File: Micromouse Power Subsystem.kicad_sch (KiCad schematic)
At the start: 9 parts, among them IC1 CH224K, J1 TYPEC-304-ACP16, J2 Conn_02x16_Odd_Even, U1 INA219AIDCNR

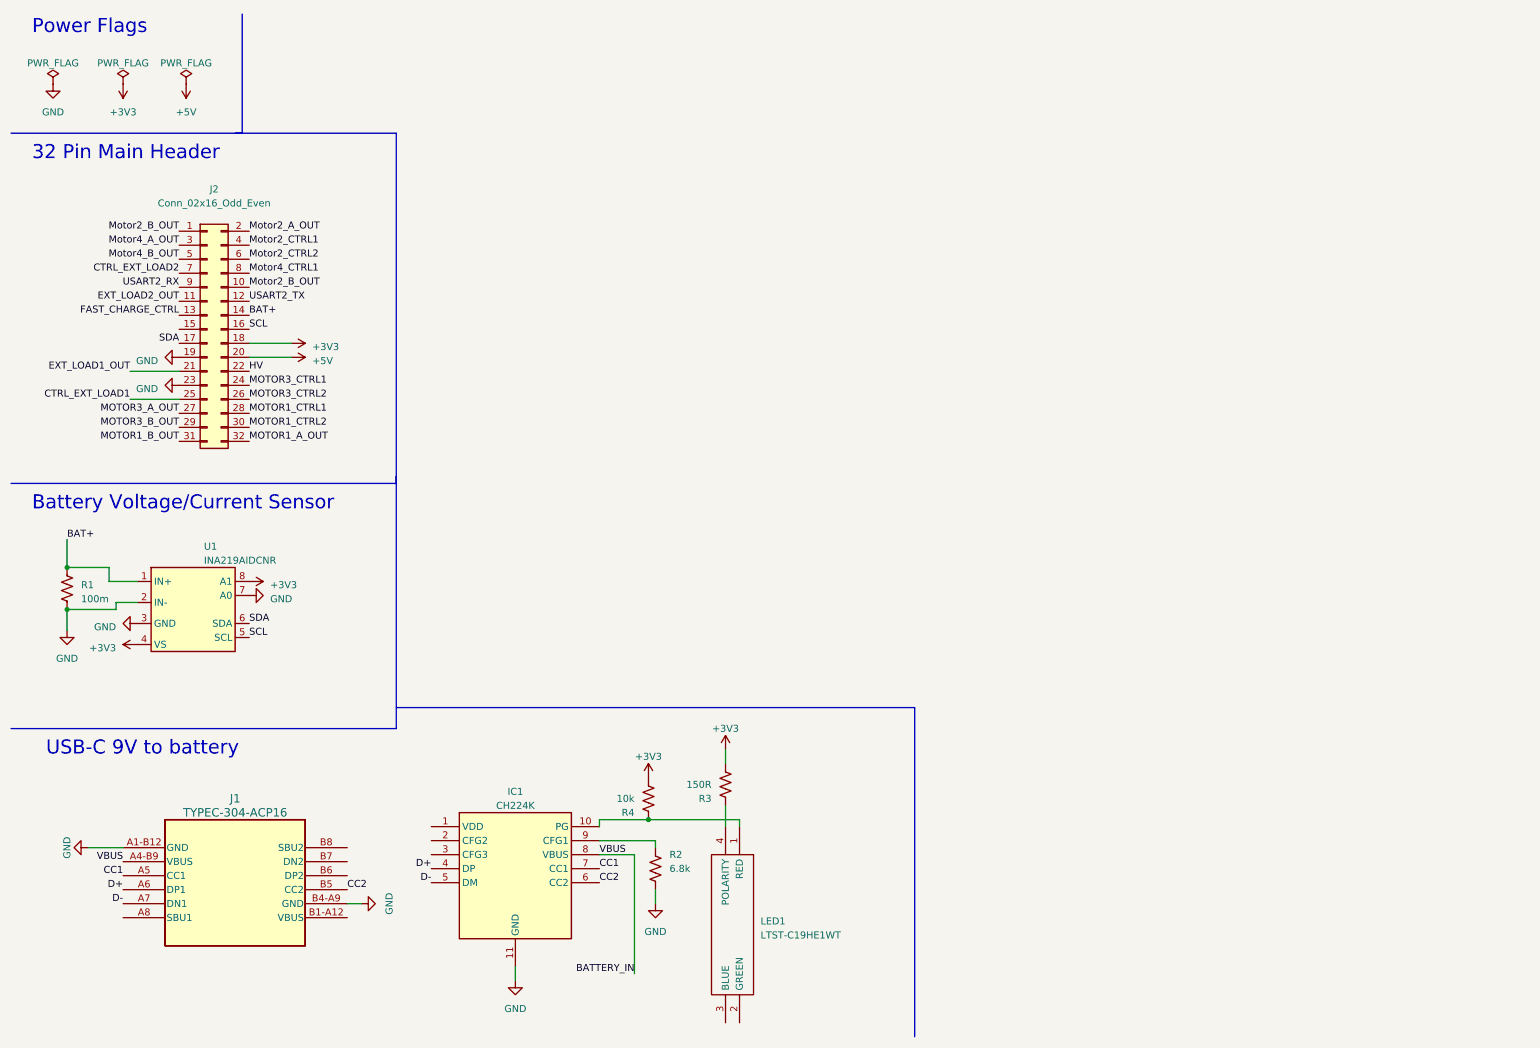
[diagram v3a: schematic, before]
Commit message: Added the charging modes as well as the charger powering the circuit when plugged in.
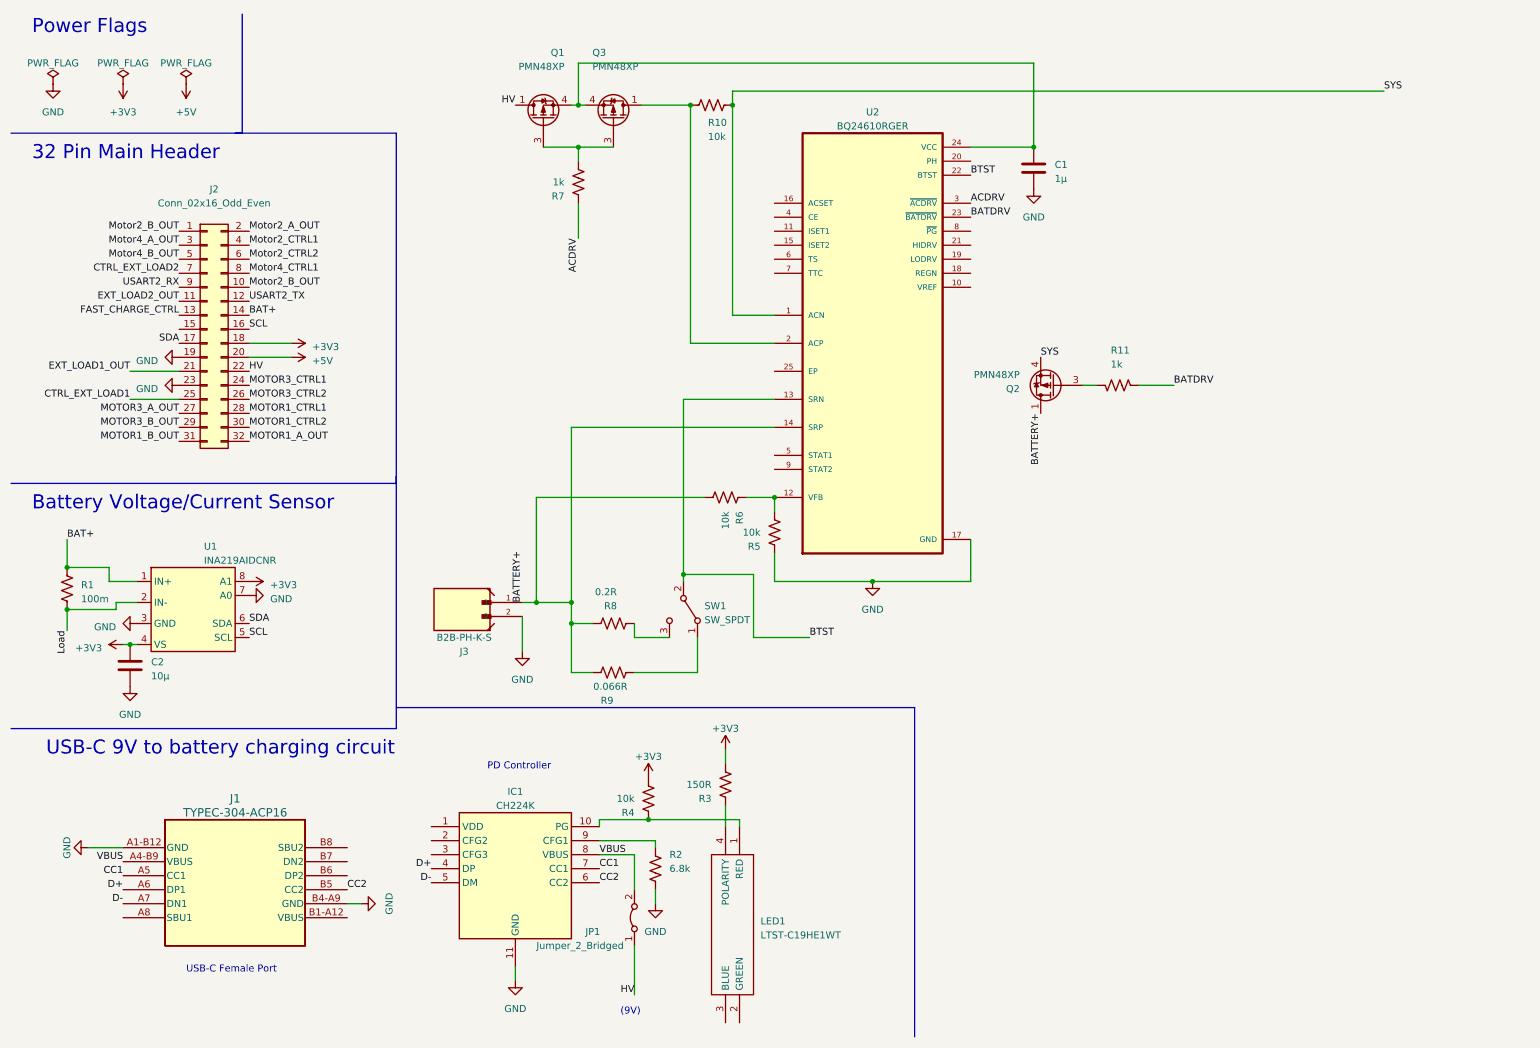
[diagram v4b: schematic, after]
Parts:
- added C1: 1µ, symbol Device:C
- added C2: 10µ, symbol Device:C
- added J3: B2B-PH-K-S, Battery JST Connector:JST_B2B-PH-K-S, symbol B2B-PH-K-S:B2B-PH-K-S
- added JP1: Jumper_2_Bridged, Jumper:SolderJumper-2_P1.3mm_Bridged2Bar_Pad1.0x1.5mm, symbol Jumper:Jumper_2_Bridged
- added Q1, Q2, Q3: PMN48XP, Package_SO:TSOP-6_1.65x3.05mm_P0.95mm, symbol Transistor_FET:PMN48XP
- added R10, R5, R6: 10k, Resistor_THT:R_Axial_DIN0204_L3.6mm_D1.6mm_P1.90mm_Vertical, symbol Device:R_US
- added R11, R7: 1k, Resistor_THT:R_Axial_DIN0204_L3.6mm_D1.6mm_P1.90mm_Vertical, symbol Device:R_US
- added R8: 0.2R, Resistor_THT:R_Axial_DIN0204_L3.6mm_D1.6mm_P1.90mm_Vertical, symbol Device:R_US
- added R9: 0.066R, Resistor_THT:R_Axial_DIN0204_L3.6mm_D1.6mm_P1.90mm_Vertical, symbol Device:R_US
- added SW1: SW_SPDT, symbol Switch:SW_SPDT
- added U2: BQ24610RGER, Battery Charger:QFN50P400X400X100-25N, symbol BQ24610RGER:BQ24610RGER
- U1: footprint Package_SO:SOIC-8_3.9x4.9mm_P1.27mm -> INA219:SOT65P280X145-8N
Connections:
- net +3V3: now also C2.1
- net GND: now also C1.2, C2.2, J3.2, R5.2, U2.17 (GND); no longer R1.1, U1.2 (IN-)
- net HV: now also JP1.1 (A), Q1.1 (D), Q1.2 (D), Q1.5 (D), Q1.6 (D)
- net BATTERY_IN renamed VBUS
- net VBUS: now also JP1.2 (B)
- new net: Q1.3 (G), Q3.3 (G), R7.1
- new net: R5.1, R6.2, U2.12 (VFB)
- new net: C1.1, Q1.4 (S), Q3.4 (S), U2.24 (VCC)
- new net: Q2.3 (G), R11.1
- new net: R9.1, SW1.1 (A)
- new net: R8.1, SW1.3 (C)
- new net: Q3.1 (D), Q3.2 (D), Q3.5 (D), Q3.6 (D), R10.1, U2.2 (ACP)
- new net ACDRV: R7.2, U2.3 (~{ACDRV})
- new net BATDRV: R11.2, U2.23 (~{BATDRV})
- new net BATTERY+: J3.1, Q2.1 (D), Q2.2 (D), Q2.5 (D), Q2.6 (D), R6.1, R8.2, R9.2, U2.14 (SRP)
- new net BTST: SW1.2 (B), U2.13 (SRN), U2.22 (BTST)
- new net Load: R1.1, U1.2 (IN-)
- new net SYS: Q2.4 (S), R10.2, U2.1 (ACN)
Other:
- note added: "(9V)"
- note added: "PD Controller"
- note added: "USB-C 9V to battery charging circuit"
- note added: "USB-C Female Port"
- note removed: "USB-C 9V to battery"

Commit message: Added the remaining connections to ground that were not in use for the battery charger
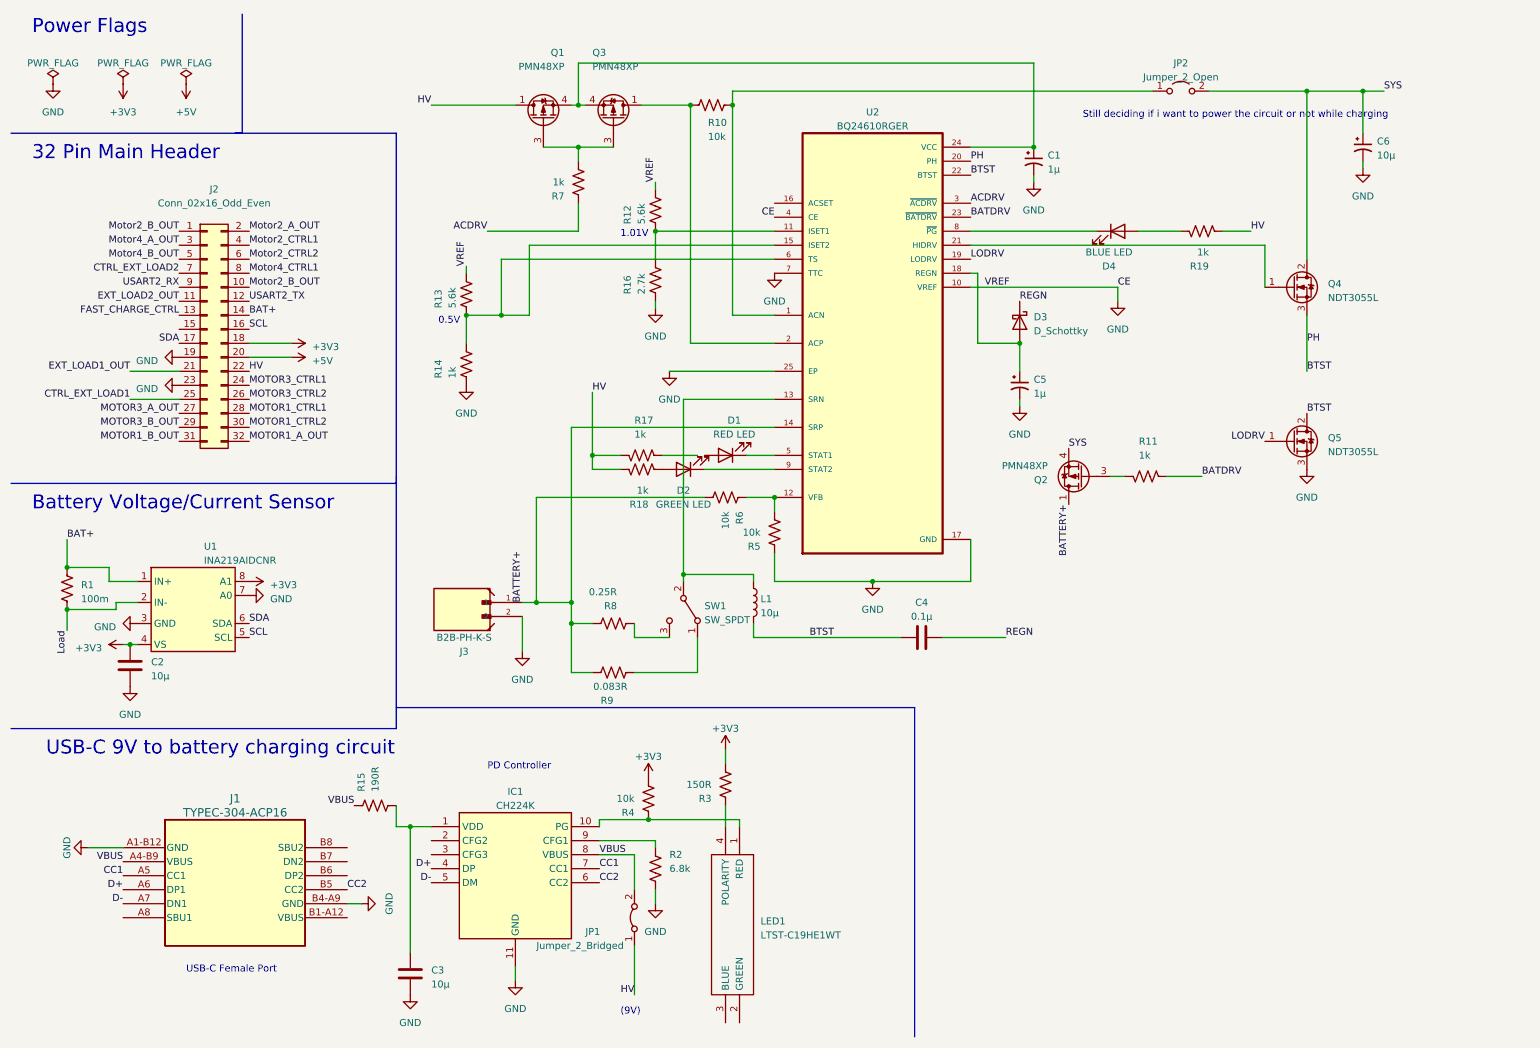
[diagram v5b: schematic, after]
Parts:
- removed C1: 1µ, symbol Device:C
- added C1, C5: 1µ, symbol Device:C_Polarized_Small_US
- added C3: 10µ, symbol Device:C
- added C4: 0.1µ, symbol Device:C
- added C6: 10µ, symbol Device:C_Polarized_Small_US
- added D1: RED LED, symbol Device:LED
- added D2: GREEN LED, symbol Device:LED
- added D3: D_Schottky, symbol Device:D_Schottky
- added D4: BLUE LED, symbol Device:LED
- added JP2: Jumper_2_Open, symbol Jumper:Jumper_2_Open
- added L1: 10µ, symbol Device:L
- added Q4, Q5: NDT3055L, Package_TO_SOT_SMD:SOT-223-3_TabPin2, symbol Transistor_FET:NDT3055L
- added R12, R13: 5.6k, Resistor_THT:R_Axial_DIN0204_L3.6mm_D1.6mm_P1.90mm_Vertical, symbol Device:R_US
- added R14, R17, R18, R19: 1k, Resistor_THT:R_Axial_DIN0204_L3.6mm_D1.6mm_P1.90mm_Vertical, symbol Device:R_US
- added R15: 190R, Resistor_THT:R_Axial_DIN0204_L3.6mm_D1.6mm_P1.90mm_Vertical, symbol Device:R_US
- added R16: 2.7k, Resistor_THT:R_Axial_DIN0204_L3.6mm_D1.6mm_P1.90mm_Vertical, symbol Device:R_US
- R8: value 0.2R -> 0.25R
- R9: value 0.066R -> 0.083R
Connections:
- net BTST: now also U2.20 (PH), C4.1, L1.2, Q4.3 (S), Q5.2 (D); no longer SW1.2 (B), U2.13 (SRN)
- net GND: now also U2.10 (VREF), U2.25 (EP), U2.4 (CE), U2.7 (TTC), C1.2, C3.2, C5.2, C6.2, Q5.3 (S), R12.2, R13.2, R14.1, R16.1
- net HV: now also R17.1, R18.2, R19.1
- net SYS: now also C6.1, JP2.2 (B), Q4.2 (D); no longer R10.2, U2.1 (ACN)
- net VBUS: now also R15.2
- net at Q1.4 (S), Q3.4 (S), U2.24 (VCC): now also C1.1
- net at U2.11 (ISET1): now also R12.1, R16.2
- net at U2.15 (ISET2): now also U2.6 (TS), R13.1, R14.2
- net at U2.18 (REGN): now also C5.1, D3.2 (A)
- net LODRV: now reaches U2.19 (LODRV)
- net LODRV: now also Q5.1 (G)
- net at U2.21 (HIDRV): now also Q4.1 (G)
- net at U2.5 (STAT1): now also D1.1 (K)
- net at U2.8 (~{PG}): now also D4.1 (K)
- net at U2.9 (STAT2): now also D2.1 (K)
- net at IC1.1 (VDD): now also C3.1, R15.1
- new net: D2.2 (A), R18.1
- new net: JP2.1 (A), R10.2, U2.1 (ACN)
- new net: L1.1, SW1.2 (B), U2.13 (SRN)
- new net: D4.2 (A), R19.2
- new net REGN: C4.2, D3.1 (K)
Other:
- note added: "0.5V"
- note added: "1.01V"
- note added: "Still deciding if i want to power the circuit or not while charging"
- moved on the sheet: Q2, R11

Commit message: Added charging circuit with new IC (BQ24074RGTR)
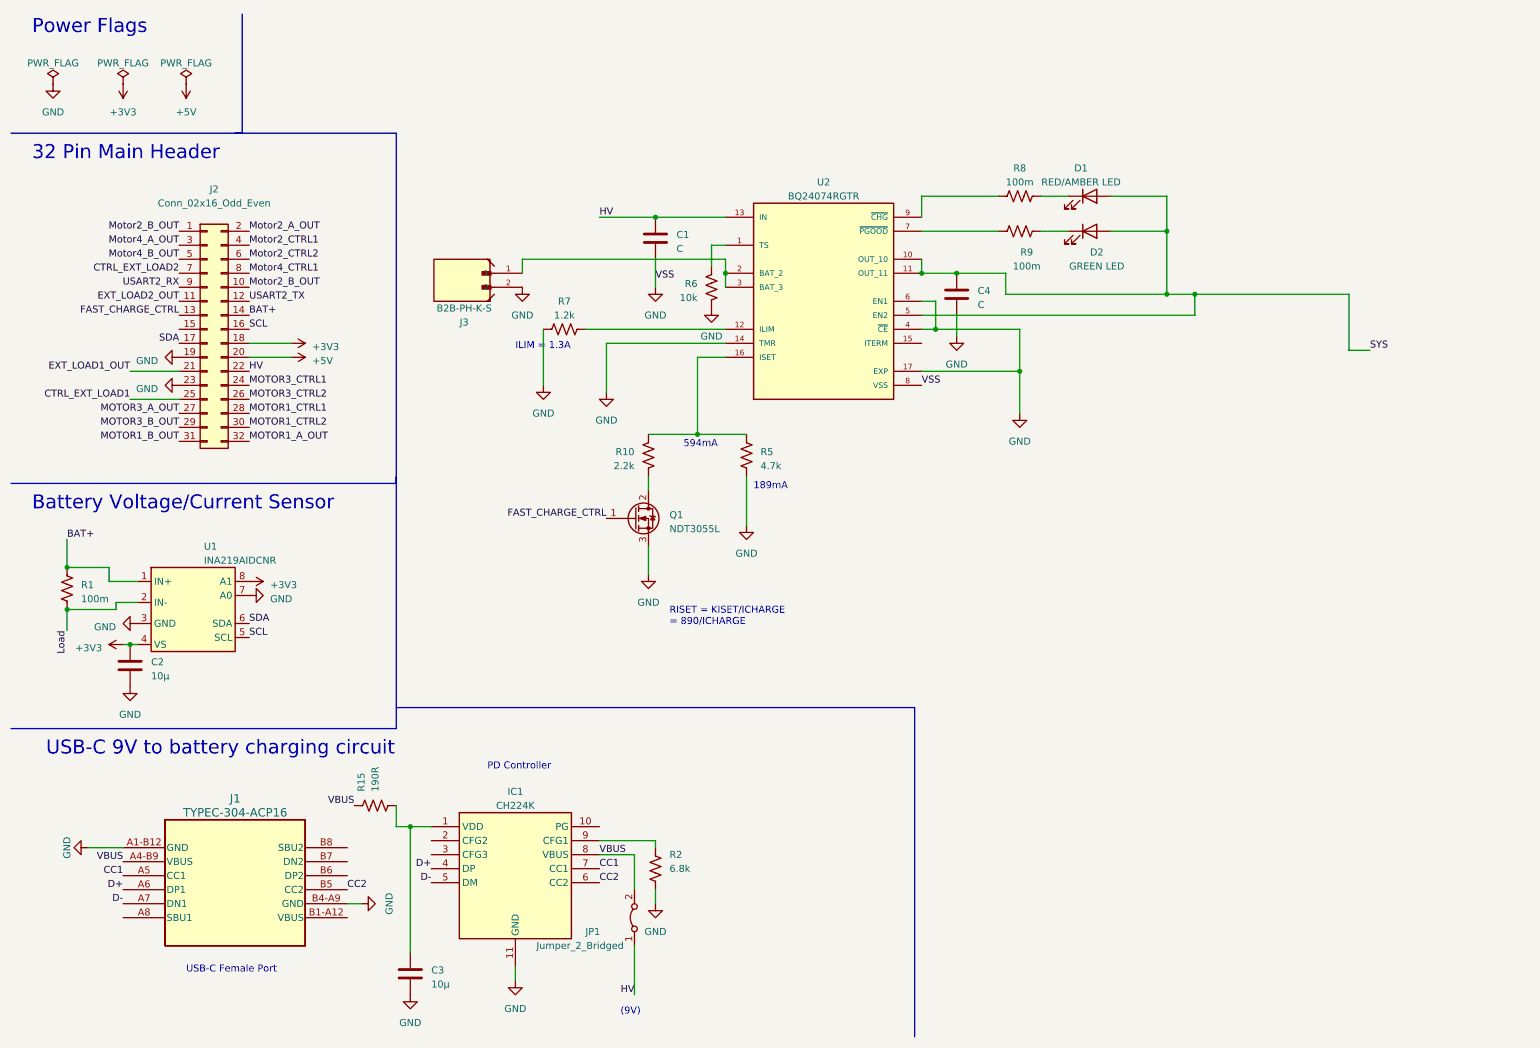
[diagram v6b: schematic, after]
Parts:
- removed C1, C5: 1µ, symbol Device:C_Polarized_Small_US
- removed C6: 10µ, symbol Device:C_Polarized_Small_US
- removed D3: D_Schottky, symbol Device:D_Schottky
- removed D4: BLUE LED, symbol Device:LED
- removed JP2: Jumper_2_Open, symbol Jumper:Jumper_2_Open
- removed L1: 10µ, symbol Device:L
- removed LED1: LTST-C19HE1WT, RGB LED:LTST-C19HE1WT, symbol LTST-C19HE1WT:LTST-C19HE1WT
- removed Q1, Q2, Q3: PMN48XP, Package_SO:TSOP-6_1.65x3.05mm_P0.95mm, symbol Transistor_FET:PMN48XP
- removed Q4, Q5: NDT3055L, Package_TO_SOT_SMD:SOT-223-3_TabPin2, symbol Transistor_FET:NDT3055L
- removed R11, R14, R17, R18, R19: 1k, Resistor_THT:R_Axial_DIN0204_L3.6mm_D1.6mm_P1.90mm_Vertical, symbol Device:R_US
- removed R12, R13: 5.6k, Resistor_THT:R_Axial_DIN0204_L3.6mm_D1.6mm_P1.90mm_Vertical, symbol Device:R_US
- removed R16: 2.7k, Resistor_THT:R_Axial_DIN0204_L3.6mm_D1.6mm_P1.90mm_Vertical, symbol Device:R_US
- removed R3: 150R, Resistor_THT:R_Axial_DIN0204_L3.6mm_D1.6mm_P1.90mm_Vertical, symbol Device:R_US
- removed R4: 10k, Resistor_THT:R_Axial_DIN0204_L3.6mm_D1.6mm_P1.90mm_Vertical, symbol Device:R_US
- removed SW1: SW_SPDT, symbol Switch:SW_SPDT
- removed U2: BQ24610RGER, Battery Charger:QFN50P400X400X100-25N, symbol BQ24610RGER:BQ24610RGER
- added C1: C, symbol Device:C
- added Q1: NDT3055L, Package_TO_SOT_SMD:SOT-223-3_TabPin2, symbol Transistor_FET:NDT3055L
- added U2: BQ24074RGTR, BQ24074RGTR:QFN50P300X300X100-17N, symbol BQ24074RGTR:BQ24074RGTR
- C4: value 0.1µ -> C
- D1: value RED LED -> RED/AMBER LED
- J3: footprint Battery JST Connector:JST_B2B-PH-K-S -> B2B-PH-K-S:JST_B2B-PH-K-S
- R10: value 10k -> 2.2k; footprint Resistor_THT:R_Axial_DIN0204_L3.6mm_D1.6mm_P1.90mm_Vertical -> Resistor_SMD:R_Shunt_Ohmite_LVK12
- R5: value 10k -> 4.7k; footprint Resistor_THT:R_Axial_DIN0204_L3.6mm_D1.6mm_P1.90mm_Vertical -> Resistor_SMD:R_Shunt_Ohmite_LVK12
- R6: footprint Resistor_THT:R_Axial_DIN0204_L3.6mm_D1.6mm_P1.90mm_Vertical -> Resistor_SMD:R_Shunt_Ohmite_LVK12
- R7: value 1k -> 1.2k; footprint Resistor_THT:R_Axial_DIN0204_L3.6mm_D1.6mm_P1.90mm_Vertical -> Resistor_SMD:R_Shunt_Ohmite_LVK12
- R8: value 0.25R -> 100m; footprint Resistor_THT:R_Axial_DIN0204_L3.6mm_D1.6mm_P1.90mm_Vertical -> Resistor_SMD:R_Shunt_Ohmite_LVK12
- R9: value 0.083R -> 100m; footprint Resistor_THT:R_Axial_DIN0204_L3.6mm_D1.6mm_P1.90mm_Vertical -> Resistor_SMD:R_Shunt_Ohmite_LVK12
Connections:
- net BTST is gone; now on net SYS: C4.1
- net REGN is gone; now on net GND: C4.2
- net FAST_CHARGE_CTRL: now also Q1.1 (G)
- net GND: now also R5.1, R6.1, R7.1, C1.2, Q1.3 (S), U2.14 (TMR), U2.17 (EXP), U2.4 (~{CE}), U2.6 (EN1), U2.8 (VSS); no longer R5.2
- net HV: now also C1.1, U2.13 (IN)
- net SYS: now also D1.2 (A), D2.2 (A), U2.10 (OUT_10), U2.11 (OUT_11), U2.5 (EN2)
- net at D2.1 (K): now also R9.2
- net at R6.2: now also U2.1 (TS); no longer R5.1
- net at R10.2: now also R5.2, U2.16 (ISET)
- net at R9.1: now also U2.7 (~{PGOOD})
- net at R8.1: now also D1.1 (K)
- net at R10.1: now also Q1.2 (D)
- net ACDRV: no longer names the net of R7.2
- net ACDRV: now also U2.12 (ILIM)
- removed net BATTERY+: J3.1, R6.1, R8.2, R9.2
- new net: J3.1, U2.2 (BAT_2), U2.3 (BAT_3)
- new net: R8.2, U2.9 (~{CHG})
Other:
- note added: "189mA"
- note added: "594mA"
- note added: "ILIM = 1.3A"
- note added: "RISET = KISET/ICHARGE = 890/ICHARGE"
- note removed: "0.5V"
- note removed: "1.01V"
- note removed: "Still deciding if i want to power the circuit or not while charging"
